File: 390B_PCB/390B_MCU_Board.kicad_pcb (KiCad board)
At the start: 2 copper layers, 78 x 80 mm, 17 parts, among them J1 Programmer Connector, J3 Motor Pins, J4 Photo R Pins, U1 ATMEGA328-PU

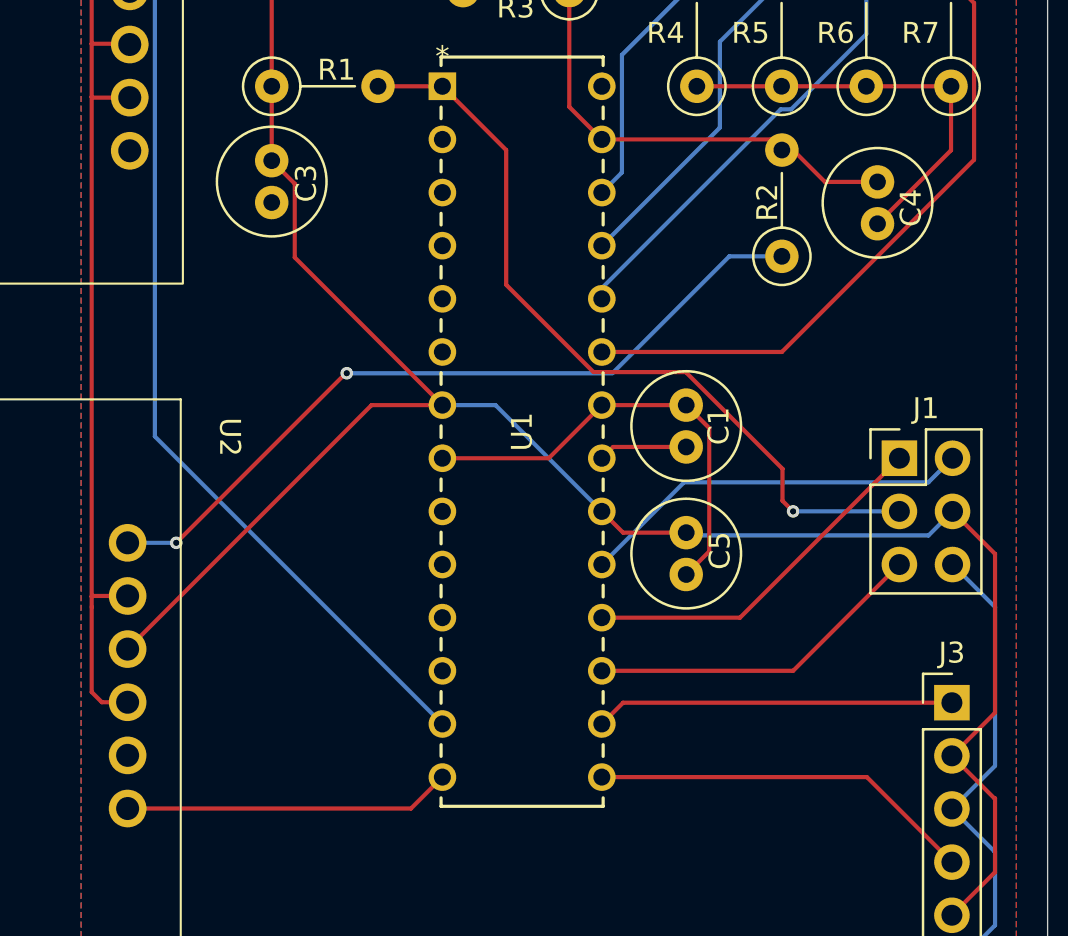
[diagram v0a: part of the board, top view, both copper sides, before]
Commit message: updates
Cap foot prints corrected
Boost connections corrected
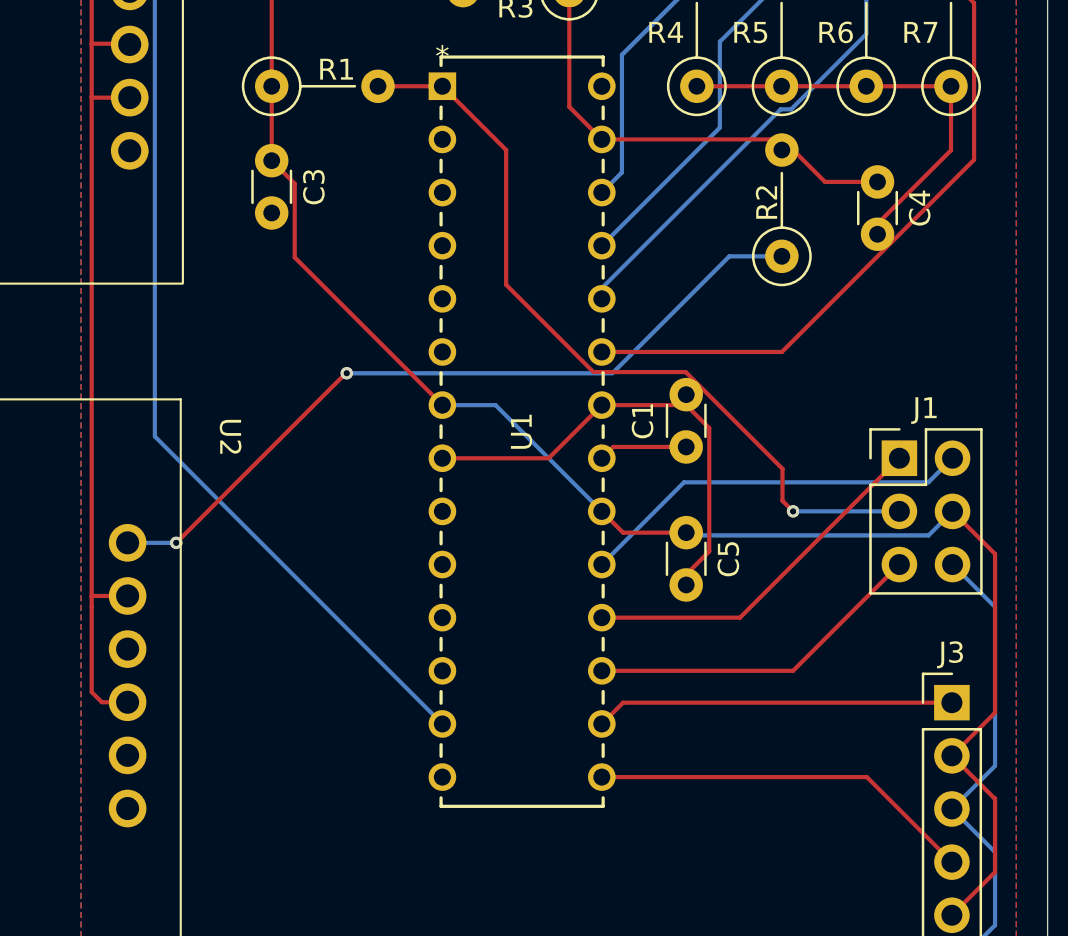
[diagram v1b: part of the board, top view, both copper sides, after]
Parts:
- C1, C3, C4, C5: footprint Capacitor_THT:C_Radial_D5.0mm_H11.0mm_P2.00mm -> Capacitor_THT:C_Disc_D3.0mm_W1.6mm_P2.50mm
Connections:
- U2 pad 3: /VCC -> /boost en
- U2 pad 6: /boost en -> /VCC
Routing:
- net /VCC: track 102.5 -> 82.6 mm
- net /boost en: track 15.7 -> 0.00 mm

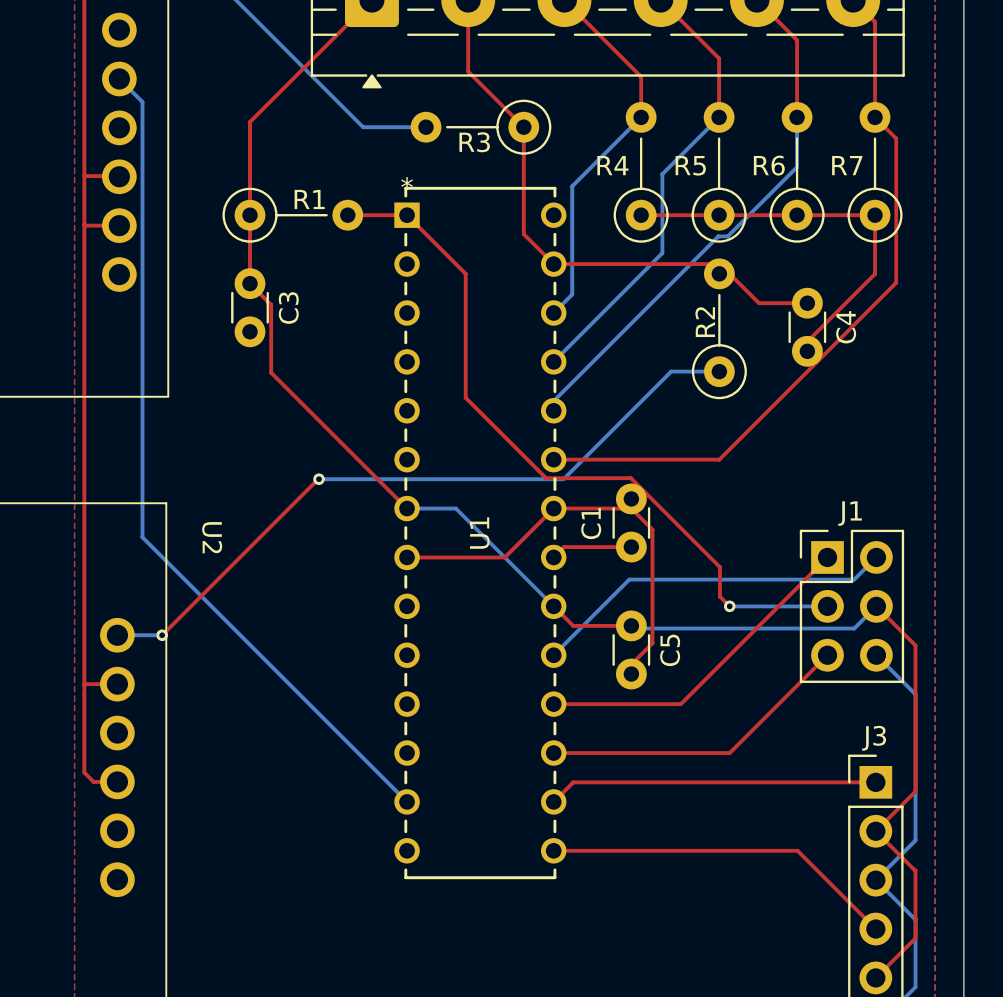
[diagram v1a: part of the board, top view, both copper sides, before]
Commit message: Major Errors Fixed
Rerouting
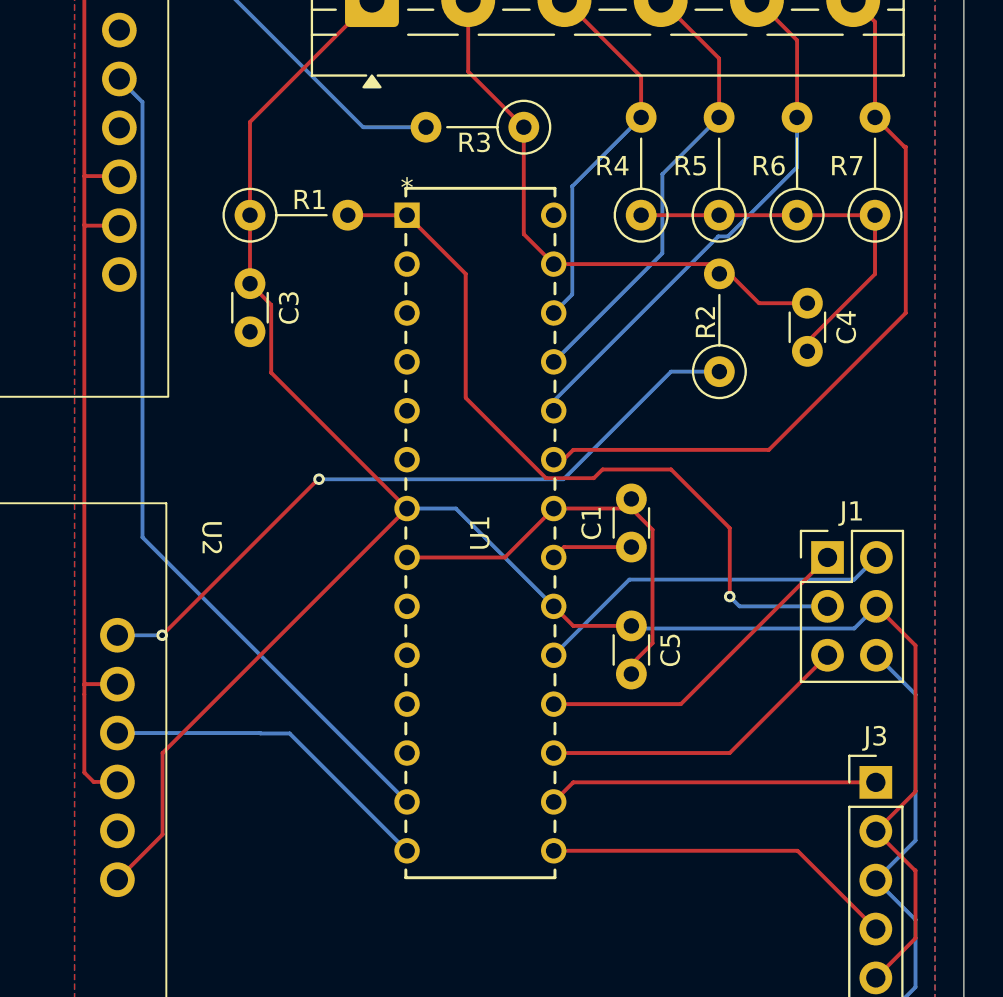
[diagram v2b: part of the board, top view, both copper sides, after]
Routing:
- net /VCC: track 82.6 -> 108.1 mm
- net /boost en: track 0.00 -> 17.6 mm
- net /PhotoR0: track 37.2 -> 38.9 mm
- net /RESET: track 38.0 -> 39.6 mm
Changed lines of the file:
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@@
+	)
+	(segment
+		(start 101.286 114.786)
+		(end 103.632 112.44)
+		(width 0.2)
+		(layer "F.Cu")
+		(net 3)
+	)
+	(segment
+		(start 103.632 108.204)
+		(end 116.332 95.504)
+		(width 0.2)
+		(layer "F.Cu")
+		(net 3)
 	)
 	(segment
@@
 	)
 	(segment
+		(start 103.632 112.44)
+		(end 103.632 108.204)
+		(width 0.2)
+		(layer "F.Cu")
+		(net 3)
+	)
+	(segment
 		(start 124.968 101.6)
 		(end 123.952 100.584)
@@
 	)
 	(segment
-		(start 132.55905 92.964)
-		(end 141.745 83.77805)
-		(width 0.2)
-		(layer "F.Cu")
-		(net 10)
-	)
-	(segment
 		(start 140.644 70.222)
 		(end 139.51 69.088)
@@
 	)
 	(segment
-		(start 141.745 83.77805)
-		(end 141.745 76.285)
+		(start 142.24 85.344)
+		(end 142.24 76.708)
+		(width 0.2)
+		(layer "F.Cu")
+		(net 10)
+	)
+	(segment
+		(start 124.968 92.456)
+		(end 135.128 92.456)
+		(width 0.2)
+		(layer "F.Cu")
+		(net 10)
+	)
+	(segment
+		(start 142.168 76.708)
+		(end 140.644 75.184)
+		(width 0.2)
+		(layer "F.Cu")
+		(net 10)
+	)
+	(segment
+		(start 124.46 92.964)
+		(end 124.968 92.456)
 		(width 0.2)
 		(layer "F.Cu")
@@
 	(segment
 		(start 123.952 92.964)
-		(end 132.55905 92.964)
-		(width 0.2)
-		(layer "F.Cu")
-		(net 10)
-	)
-	(segment
-		(start 141.745 76.285)
-		(end 140.644 75.184)
+		(end 124.46 92.964)
+		(width 0.2)
+		(layer "F.Cu")
+		(net 10)
+	)
+	(segment
+		(start 135.128 92.456)
+		(end 142.24 85.344)
+		(width 0.2)
+		(layer "F.Cu")
+		(net 10)
+	)
+	(segment
+		(start 142.24 76.708)
+		(end 142.168 76.708)
 		(width 0.2)
 		(layer "F.Cu")
@@
 	)
 	(segment
-		(start 127.96445 93.9254)
-		(end 132.589525 98.550475)
-		(width 0.2)
-		(layer "F.Cu")
-		(net 19)
-	)
-	(segment
-		(start 133.096 100.584)
-		(end 132.588 100.076)
-		(width 0.2)
-		(layer "F.Cu")
-		(net 19)
-	)
-	(segment
-		(start 132.588 98.552)
-		(end 132.589525 98.550475)
-		(width 0.2)
-		(layer "F.Cu")
-		(net 19)
-	)
-	(segment
-		(start 123.553775 93.9254)
-		(end 127.96445 93.9254)
+		(start 119.38 83.312)
+		(end 119.38 89.751625)
+		(width 0.2)
+		(layer "F.Cu")
+		(net 19)
+	)
+	(segment
+		(start 133.096 96.52)
+		(end 133.096 100.076)
+		(width 0.2)
+		(layer "F.Cu")
+		(net 19)
+	)
+	(segment
+		(start 116.332 80.264)
+		(end 119.38 83.312)
+		(width 0.2)
+		(layer "F.Cu")
+		(net 19)
+	)
+	(segment
+		(start 126.492 93.472)
+		(end 130.048 93.472)
+		(width 0.2)
+		(layer "F.Cu")
+		(net 19)
+	)
+	(segment
+		(start 130.048 93.472)
+		(end 133.096 96.52)
 		(width 0.2)
 		(layer "F.Cu")
@@
 	)
 	(segment
-		(start 119.38 83.312)
-		(end 119.38 89.751625)
-		(width 0.2)
-		(layer "F.Cu")
-		(net 19)
-	)
-	(segment
-		(start 132.588 100.076)
-		(end 132.588 98.552)
-		(width 0.2)
-		(layer "F.Cu")
-		(net 19)
-	)
-	(segment
-		(start 116.332 80.264)
-		(end 119.38 83.312)
+		(start 123.553775 93.9254)
+		(end 126.0386 93.9254)
+		(width 0.2)
+		(layer "F.Cu")
+		(net 19)
+	)
+	(segment
+		(start 126.0386 93.9254)
+		(end 126.492 93.472)
 		(width 0.2)
 		(layer "F.Cu")
@@
 	)
 	(via
-		(at 133.096 100.584)
+		(at 133.096 100.076)
 		(size 0.6)
 		(drill 0.3)
@@
 	(segment
 		(start 138.176 100.584)
-		(end 133.096 100.584)
+		(end 133.604 100.584)
+		(width 0.2)
+		(layer "B.Cu")
+		(net 19)
+	)
+	(segment
+		(start 133.604 100.584)
+		(end 133.096 100.076)
 		(width 0.2)
 		(layer "B.Cu")
@@
 	)
 	(segment
+		(start 108.69 107.166)
+		(end 108.712 107.188)
+		(width 0.2)
+		(layer "B.Cu")
+		(net 25)
+	)
+	(segment
+		(start 110.236 107.188)
+		(end 116.332 113.284)
+		(width 0.2)
+		(layer "B.Cu")
+		(net 25)
+	)
+	(segment
+		(start 101.286 107.166)
+		(end 108.69 107.166)
+		(width 0.2)
+		(layer "B.Cu")
+		(net 25)
+	)
+	(segment
+		(start 108.712 107.188)
+		(end 110.236 107.188)
+		(width 0.2)
+		(layer "B.Cu")
+		(net 25)
+	)
+	(segment
